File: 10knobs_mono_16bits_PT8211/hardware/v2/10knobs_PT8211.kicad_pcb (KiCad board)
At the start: 2 copper layers, 48 parts, among them J1 Conn_01x06_Female, U1 PT8211, U2 BluePill_STM32F103C, U3 6N138, U4 LM358

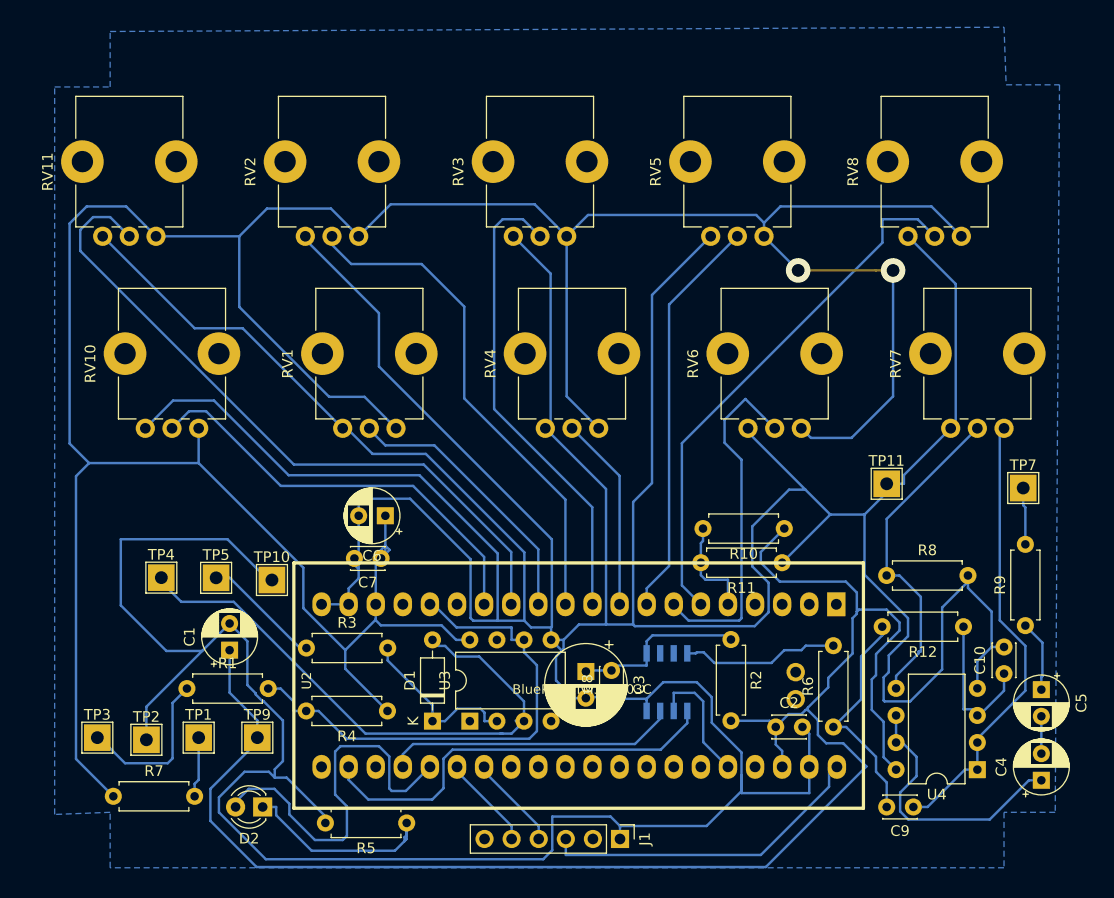
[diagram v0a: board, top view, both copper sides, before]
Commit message: Moved to seperate folders
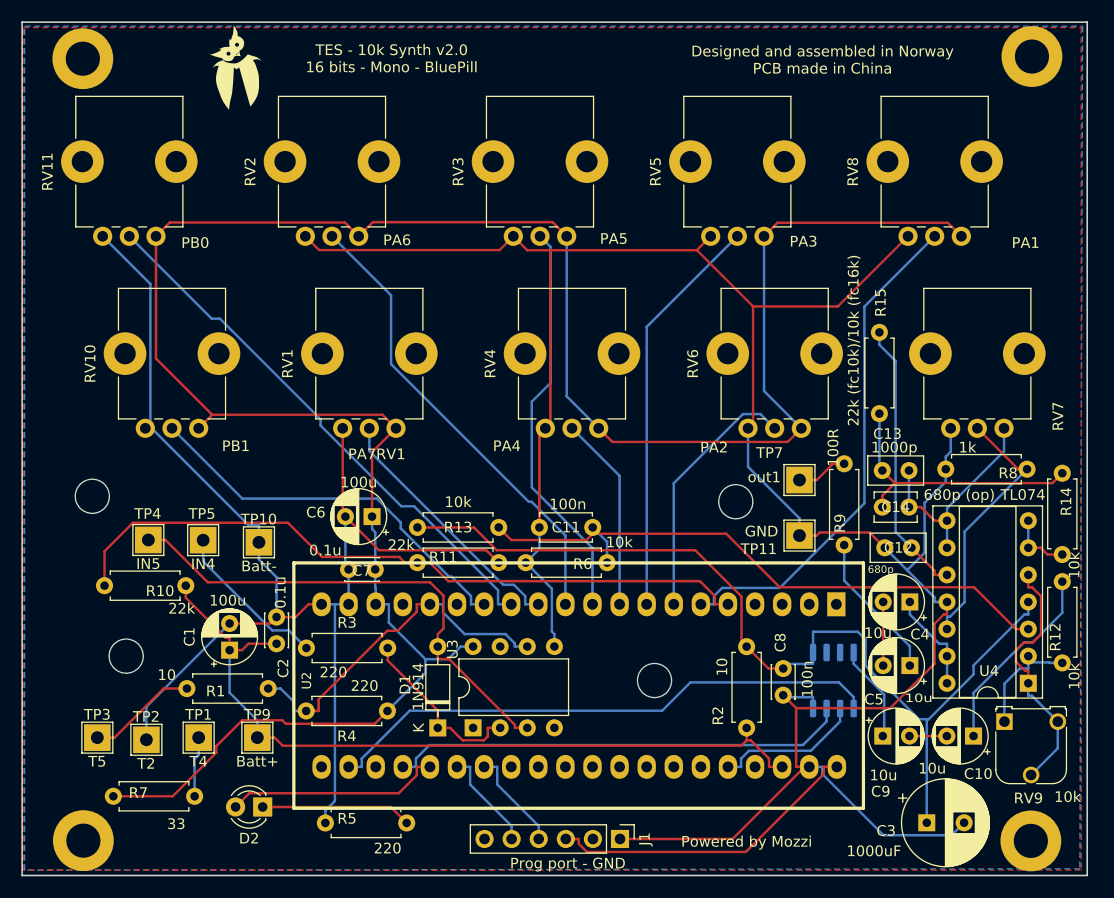
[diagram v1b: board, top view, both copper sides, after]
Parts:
- added C11: 100n, Capacitor_THT:C_Disc_D4.7mm_W2.5mm_P5.00mm, F.Cu at (91.4, 66.3)
- added C12: 680p, Capacitor_THT:C_Disc_D5.0mm_W2.5mm_P2.50mm, F.Cu at (123.8, 68.2)
- added C13: 1000p, Capacitor_THT:C_Disc_D5.0mm_W2.5mm_P2.50mm, F.Cu at (123.6, 61.0)
- added C14: 680p (op), Capacitor_THT:C_Disc_D3.8mm_W2.6mm_P2.50mm, F.Cu at (126.1, 64.4)
- added G***: LOGO, PCB_symbols:owl_7x10, F.Cu at (63.0, 23.4)
- added G***: LOGO, PCB_symbols:owl_F_50x70, B.Cu at (66.9, 55.5)
- added H1: MountingHole, MountingHole:MountingHole_3.2mm_M3, F.Cu at (52.7, 78.4)
- added H2: MountingHole, MountingHole:MountingHole_3.2mm_M3, F.Cu at (102.2, 80.6)
- added H3: MountingHole, MountingHole:MountingHole_3.2mm_M3_ISO7380_Pad, F.Cu at (137.5, 95.7)
- added H4: MountingHole, MountingHole:MountingHole_3.2mm_M3_ISO7380_Pad, F.Cu at (48.6, 22.4)
- added H5: MountingHole, MountingHole:MountingHole_3.2mm_M3, F.Cu at (109.9, 63.9)
- added H6: MountingHole, MountingHole:MountingHole_3.2mm_M3_ISO7380_Pad, F.Cu at (48.7, 95.7)
- added H7: MountingHole, MountingHole:MountingHole_3.2mm_M3_ISO7380_Pad, F.Cu at (137.6, 22.1)
- added H8: MountingHole, MountingHole:MountingHole_3.2mm_M3, F.Cu at (49.5, 63.4)
- added R13: 10k, Resistor_THT:R_Axial_DIN0207_L6.3mm_D2.5mm_P7.62mm_Horizontal, F.Cu at (87.6, 66.3)
- added R14: 10k, Resistor_THT:R_Axial_DIN0207_L6.3mm_D2.5mm_P7.62mm_Horizontal, F.Cu at (140.5, 61.2)
- added R15: 22k (fc10k)/10k (fc16k), Resistor_THT:R_Axial_DIN0207_L6.3mm_D2.5mm_P7.62mm_Horizontal, F.Cu at (123.3, 55.6)
- added RV9: 10k, Potentiometer_THT:Potentiometer_Runtron_RM-065_Vertical, F.Cu at (135.0, 84.5)
- C1: value 100u_chem -> 100u
- C10: value 680p -> 10u; footprint Capacitor_THT:C_Disc_D3.0mm_W2.0mm_P2.50mm -> Capacitor_THT:CP_Radial_D5.0mm_P2.50mm
- C2, C7: value 0.1u ceram -> 0.1u
- C3: footprint Capacitor_THT:CP_Radial_D7.5mm_P2.50mm -> Capacitor_THT:CP_Radial_D8.0mm_P3.50mm
- C6: value 100u chem -> 100u
- C9: value 1000p -> 10u; footprint Capacitor_THT:C_Disc_D3.0mm_W2.0mm_P2.50mm -> Capacitor_THT:CP_Radial_D5.0mm_P2.50mm
- J1: value Conn_01x06_Female -> Prog port - GND
- U1: footprint Package_SO:SOIC-8_3.9x4.9mm_P1.27mm -> Package_SO:SOP-8_3.9x4.9mm_P1.27mm
- U2: value BluePill_STM32F103C -> BluePill_STM32F103C_breadboard_friendly; footprint BluePill_breakouts:BluePill_STM32F103C -> BluePill_breakouts:BluePill_STM32F103C_breadboard_friendly
- U4: value LM358 -> TL074; footprint Package_DIP:DIP-8_W7.62mm -> Package_DIP:DIP-14_W7.62mm_Socket
- moved R10 56.4 mm to (58.3, 71.8)
- moved C2 47.4 mm to (66.8, 77.2), turned to 90 degrees
- moved C3 35.0 mm to (127.8, 94.0), turned to 0 degrees
- moved R6 32.7 mm to (90.2, 69.6), turned to 0 degrees
- moved R11 26.6 mm to (87.6, 69.6)
- moved TP7 21.0 mm to (115.8, 61.8)
- moved C4 20.8 mm to (126.2, 73.3), turned to 180 degrees
- moved R9 18.6 mm to (120.0, 67.9)
- moved R8 16.5 mm to (137.2, 60.8), turned to 180 degrees
- moved C8 16.1 mm to (114.3, 82.0)
- moved U1 15.6 mm to (119.0, 80.6)
- moved C5 12.5 mm to (126.2, 79.2), turned to 180 degrees
- moved R12 10.2 mm to (140.5, 71.4), turned to -90 degrees
- moved TP11 9.51 mm to (115.8, 67.1)
- moved U4 9.40 mm to (137.3, 80.9)
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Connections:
- C10 pad 2: GND -> Net-(C10-Pad2)
- C3 pad 1: Net-(C3-Pad1) -> /filtered_vcc
- C8 pad 2: Net-(C3-Pad1) -> /filtered_vcc
- C9 pad 1: DAC_out -> Net-(C9-Pad1)
- C9 pad 2: Net-(C9-Pad2) -> Net-(C10-Pad2)
- J1 pad 2: (no net) -> unconnected-(J1-Pad2)
- J1 pad 6: (no net) -> unconnected-(J1-Pad6)
- R12 pad 2: Net-(C9-Pad2) -> Net-(R12-Pad2)
- R2 pad 1: Net-(C3-Pad1) -> /filtered_vcc
- R6 pad 1: Net-(C9-Pad2) -> GND
- R6 pad 2: Net-(R6-Pad2) -> Net-(C11-Pad2)
- RV7 pad 1: DAC_out -> /filter_out
- U1 pad 5: Net-(C3-Pad1) -> /filtered_vcc
- U1 pad 6: (no net) -> unconnected-(U1-Pad6)
- U1 pad 7: (no net) -> unconnected-(U1-Pad7)
- U1 pad 8: Net-(R6-Pad2) -> Net-(C9-Pad1)
- U2 pad 1: (no net) -> unconnected-(U2-Pad1)
- U2 pad 15: (no net) -> unconnected-(U2-Pad15)
- U2 pad 17: (no net) -> unconnected-(U2-Pad17)
- U2 pad 2: (no net) -> unconnected-(U2-Pad2)
- U2 pad 21: (no net) -> unconnected-(U2-Pad21)
- U2 pad 23: (no net) -> unconnected-(U2-Pad23)
- U2 pad 28: (no net) -> unconnected-(U2-Pad28)
- U2 pad 29: (no net) -> unconnected-(U2-Pad29)
- U2 pad 3: (no net) -> unconnected-(U2-Pad3)
- U2 pad 30: (no net) -> unconnected-(U2-Pad30)
- U2 pad 31: (no net) -> unconnected-(U2-Pad31)
- U2 pad 32: (no net) -> unconnected-(U2-Pad32)
- U2 pad 33: (no net) -> unconnected-(U2-Pad33)
- U2 pad 34: (no net) -> unconnected-(U2-Pad34)
- U2 pad 35: (no net) -> unconnected-(U2-Pad35)
- U2 pad 37: (no net) -> unconnected-(U2-Pad37)
- U2 pad 4: (no net) -> unconnected-(U2-Pad4)
- U3 pad 1: (no net) -> unconnected-(U3-Pad1)
- U3 pad 4: (no net) -> unconnected-(U3-Pad4)
- U3 pad 7: (no net) -> unconnected-(U3-Pad7)
- U4 pad 2: DAC_out -> Net-(R12-Pad2)
- U4 pad 3: Net-(C10-Pad1) -> Net-(C11-Pad2)
- U4 pad 4: GND -> /filtered_vcc
- U4 pad 5: Net-(R8-Pad1) -> DAC_out
- U4 pad 6: Net-(C4-Pad1) -> Net-(R14-Pad2)
- U4 pad 7: Net-(C4-Pad1) -> Net-(R14-Pad2)
- U4 pad 8: batt+ -> /filter_out
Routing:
- net GND: track 594.4 -> 357.3 mm
- net /filtered_vcc: track 0.00 -> 88.7 mm
- net +3V3: track 303.9 -> 223.7 mm, vias 2 -> 0
- net batt+: track 154.3 -> 74.3 mm
- net Net-(C11-Pad2): track 0.00 -> 58.5 mm
- net Net-(R10-Pad2): track 9.47 -> 66.4 mm
- net Net-(C12-Pad2): track 0.00 -> 26.0 mm
- net Net-(C13-Pad1): track 0.00 -> 25.9 mm
- net Net-(C9-Pad2): track 21.6 -> 0.00 mm
- net /filter_out: track 0.00 -> 20.9 mm
- net DAC_out: track 42.5 -> 24.0 mm
- net Net-(C3-Pad1): track 16.5 -> 0.00 mm
- net Net-(C4-Pad1): track 25.9 -> 9.50 mm
- net Net-(D2-Pad2): track 36.0 -> 20.2 mm
- net Net-(U1-Pad3): track 27.4 -> 43.1 mm
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- added copper zone on F.Cu, net GND
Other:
- board outline added: 99.8 x 80 mm
- net class Default removed
- net class easy removed
- rule pad_to_mask_clearance: 0.051 -> 0
- board text added: "Designed and assembled in Norway PCB made in China"
- board text added: "Powered by Mozzi"
- board text added: "TES - 10k Synth v2.0 16 bits - Mono - BluePill"
